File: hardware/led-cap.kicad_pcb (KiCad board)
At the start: 2 copper layers, 76.2 x 17.8 mm, 12 parts, among them IC1 ATTINY20-X, K1 CONN_3, P1 battery, P2 pgrm, Q1 IRLML2402PbF, U1 MMA7660

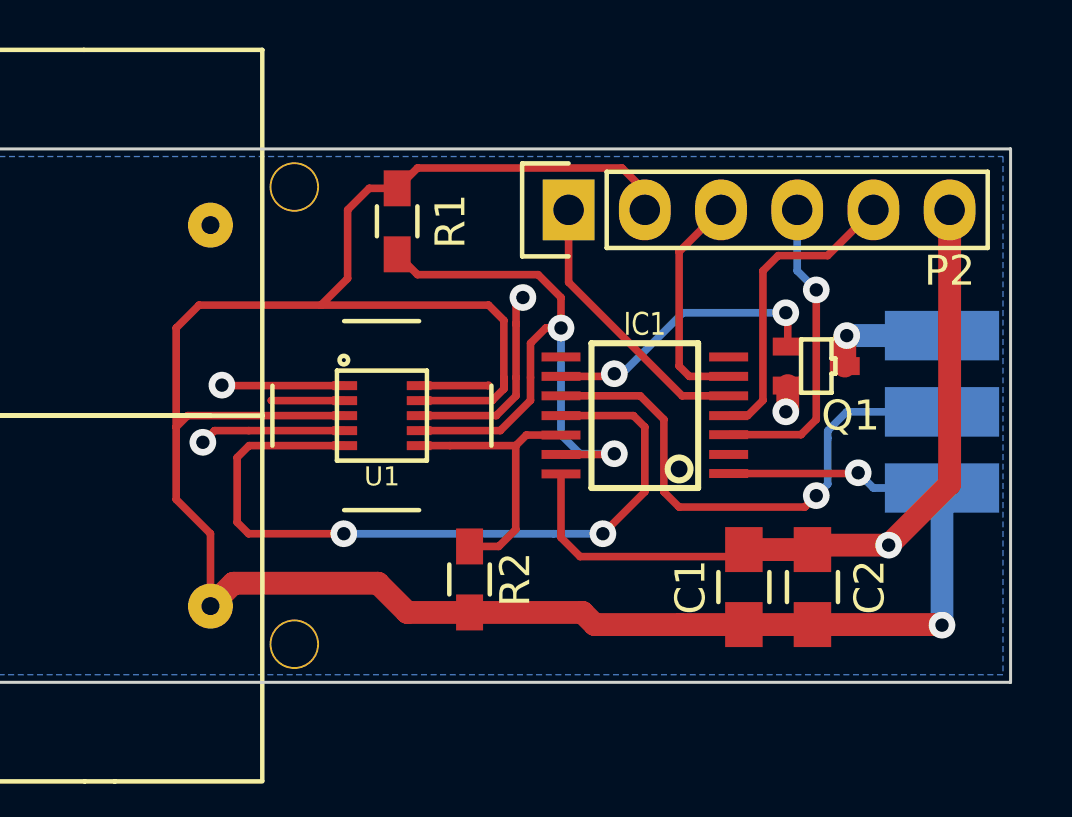
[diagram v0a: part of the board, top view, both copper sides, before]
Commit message: Fixing the mosfet
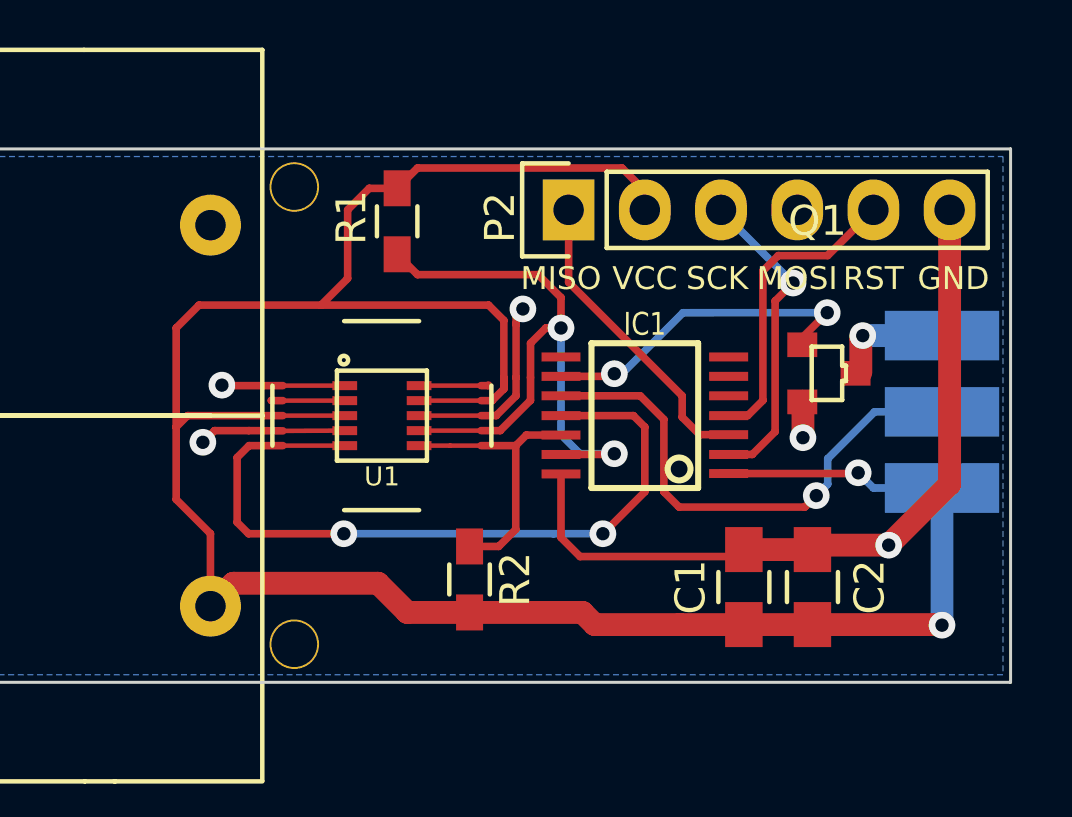
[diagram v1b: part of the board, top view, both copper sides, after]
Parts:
- P2: value pgrm -> TPI pgrm
- Q1: footprint SMD_Packages:SOT-323 -> mods.pretty:SOT-323-b
- moved Q1 1.33 mm to (187.9, 76.1), turned to 270 degrees
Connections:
- IC1 pad 2: Net-(IC1-Pad2) -> /CLOCK
- IC1 pad 3: /MOSI -> /DATA
- IC1 pad 5: /MISO -> Net-(IC1-Pad5)
- IC1 pad 6: /SCLK -> Net-(IC1-Pad6)
- P2 pad 1: /MISO -> /DATA
- P2 pad 3: /SCLK -> /CLOCK
- P2 pad 4: /MOSI -> Net-(P2-Pad4)
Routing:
- net /CLOCK: track 0.00 -> 10.5 mm, vias 0 -> 1
- net /MOSI: track 10.4 -> 0.00 mm, vias 1 -> 0
- net /DATA: track 0.00 -> 10.3 mm
- net /MISO: track 9.31 -> 0.00 mm
- net /SCLK: track 7.32 -> 0.00 mm
- net /LED_CTRL: track 9.65 -> 11.4 mm
- net /LED_DATA: track 20.5 -> 20.0 mm
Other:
- board text added: "GND"
- board text added: "MISO"
- board text added: "MOSI"
- board text added: "RST"
- board text added: "SCK"
- board text added: "VCC"

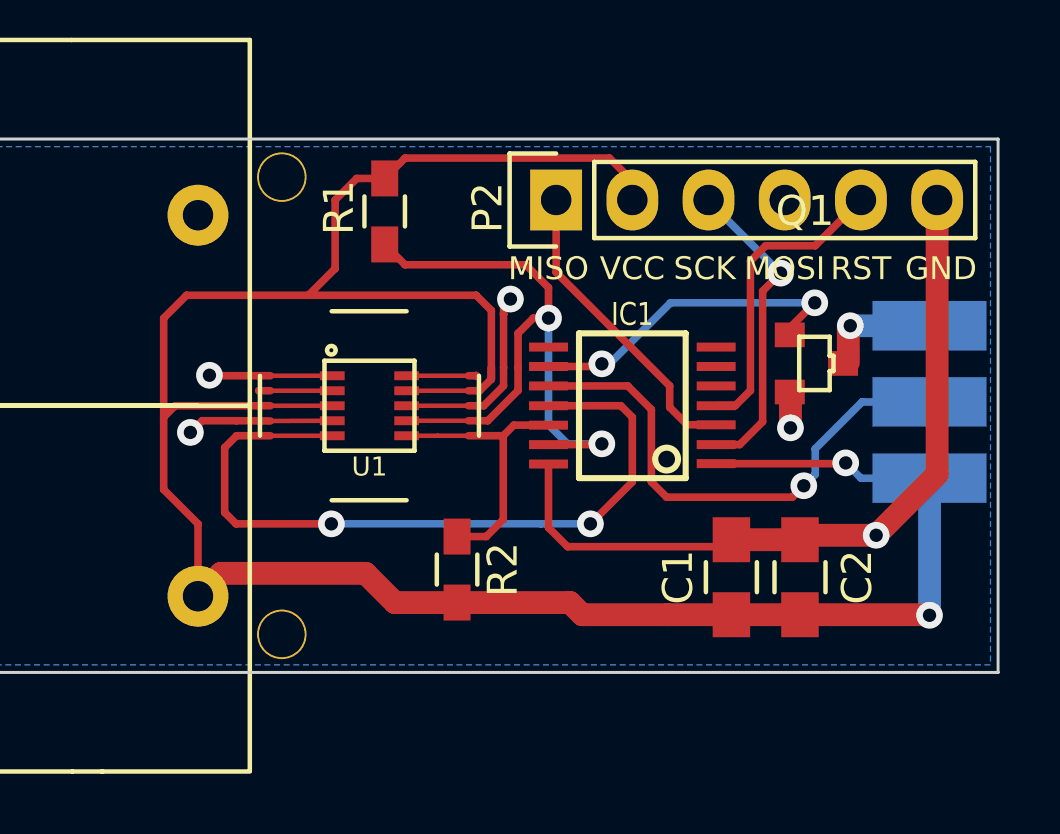
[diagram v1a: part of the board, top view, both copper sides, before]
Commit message: Fixed pcb and schematic for TPI and new LED strips
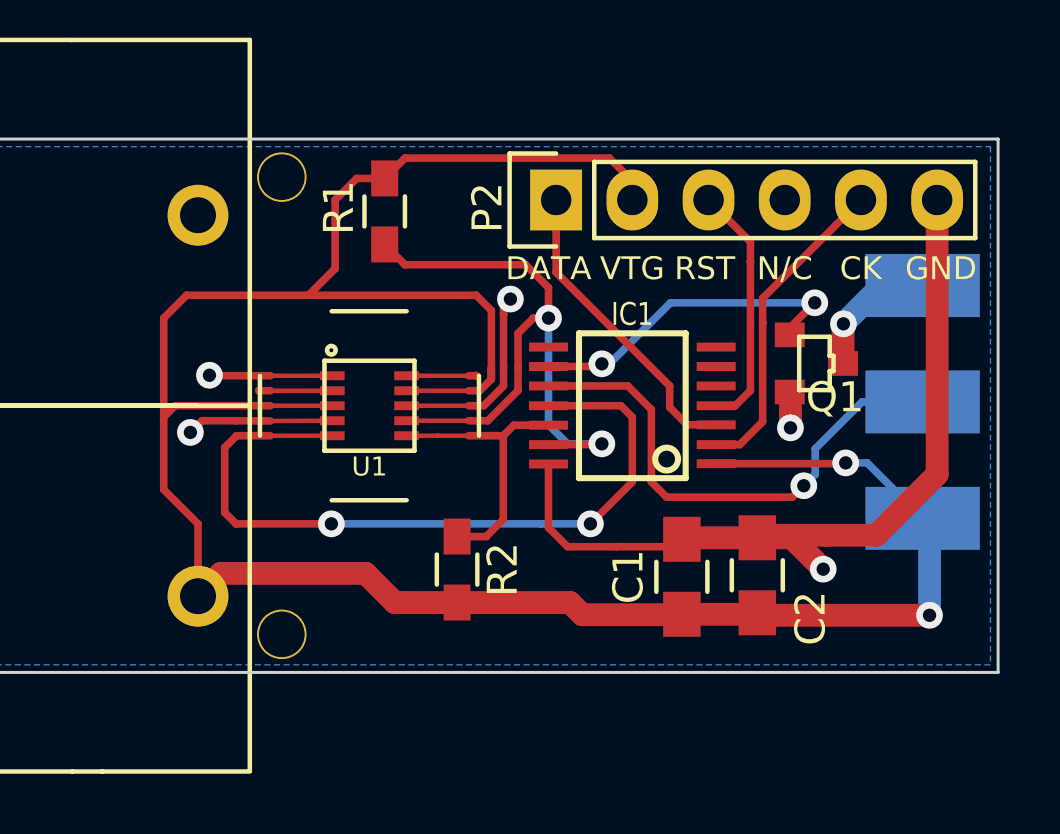
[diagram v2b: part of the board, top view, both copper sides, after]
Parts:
- K1: footprint mods.pretty:GS3 -> mods.pretty:LEDS
- moved C1 1.65 mm to (182.5, 83.2)
- moved C2 1.42 mm to (185.0, 83.1)
- moved K1 0.23 mm to (190.5, 77.3)
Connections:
- IC1 pad 2: /CLOCK -> /CLK
- P2 pad 3: /CLOCK -> /RST
- P2 pad 5: /RST -> /CLK
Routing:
- net /CLK: track 0.00 -> 10.7 mm
- net /CLOCK: track 10.5 -> 0.00 mm, vias 1 -> 0
- net GND: track 42.3 -> 44.9 mm
- net /RST: track 10.2 -> 8.35 mm
- net VCC: track 85.1 -> 84.3 mm
- net /LED_GND: track 3.90 -> 4.50 mm
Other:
- board text added: "CK"
- board text added: "DAT"
- board text added: "DATA"
- board text added: "N/C"
- board text added: "Spring 2015 Butler Fund"
- board text added: "UMAINE ECE 498"
- board text added: "VTG"
- board text removed: "MISO"
- board text removed: "MOSI"
- board text removed: "SCK"
- board text removed: "UMAINE ECE 498 Spring 2015 Butler Fund"

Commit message: Contains files as submitted to PCBCart
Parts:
- added 1pin: VAL**, mods.pretty:1pin, F.Cu at (191.8, 85.1)
- added 1pin: VAL**, mods.pretty:1pin, F.Cu at (118.7, 84.7)
- added 1pin: VAL**, mods.pretty:1pin, F.Cu at (118.8, 70.3)
- added 1pin: VAL**, mods.pretty:1pin, F.Cu at (142.5, 77.5)
- moved Q1 0.27 mm to (188.1, 76.0)
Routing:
- net VCC: track 84.3 -> 83.0 mm
- net /LED_CTRL: track 11.4 -> 10.4 mm
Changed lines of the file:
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@@
     (links 28)
     (no_connects 0)
-    (area 116.789999 68.529999 193.090001 86.410001)
+    (area 116.45569 65.050599 197.579962 89.889401)
     (thickness 1.6)
     (drawings 15)
     (tracks 177)
     (zones 0)
-    (modules 12)
+    (modules 16)
     (nets 19)
   )
@@
     (pcbplotparams
       (layerselection 0x010f0_80000001)
-      (usegerberextensions false)
+      (usegerberextensions true)
       (excludeedgelayer true)
       (linewidth 0.100000)
@@
     )
   )
-  (module mods.pretty:SOT-323-b placed (layer F.Cu)
-    (at 187.8711 76.0603 270)
-    (tags "SMD SOT")
-    (attr smd)
-    (fp_text reference Q1 (at 1.1303 0.2667 360) (layer F.SilkS)
-      (effects (font (size 1 1) (thickness 0.15)))
-    )
-    (fp_text value IRLML2402PbF (at 0 -3.81 270) (layer F.SilkS) hide
-      (effects (font (size 1 1) (thickness 0.15)))
-    )
-    (fp_line (start 0.254 0.4445) (end 0.889 0.4445) (layer F.SilkS) (width 0.15))
-    (fp_line (start 0.889 0.4445) (end 0.889 1.4605) (layer F.SilkS) (width 0.15))
-    (fp_line (start -0.889 1.4605) (end -0.889 0.4445) (layer F.SilkS) (width 0.15))
-    (fp_line (start -0.889 0.4445) (end -0.254 0.4445) (layer F.SilkS) (width 0.15))
-    (fp_line (start 0.254 0.3175) (end 0.254 0.4445) (layer F.SilkS) (width 0.15))
-    (fp_line (start -0.254 0.4445) (end -0.254 0.3175) (layer F.SilkS) (width 0.15))
-    (fp_line (start 0.889 1.4605) (end -0.889 1.4605) (layer F.SilkS) (width 0.15))
-    (fp_line (start -0.254 0.3175) (end 0.254 0.3175) (layer F.SilkS) (width 0.15))
-    (pad 2 smd rect (at 0.9525 1.77546 270) (size 0.82296 1.00076) (layers F.Cu F.Paste F.Mask)
-      (net 2 GND))
-    (pad 1 smd rect (at -0.9525 1.77546 270) (size 0.82296 1.00076) (layers F.Cu F.Paste F.Mask)
-      (net 6 /LED_CTRL))
-    (pad 3 smd rect (at 0 0 270) (size 0.82296 1.00076) (layers F.Cu F.Paste F.Mask)
-      (net 11 /LED_GND))
-    (model SMD_Packages/SOT-323.wrl
-      (at (xyz 0 0 0.001))
-      (scale (xyz 0.3937 0.3937 0.3937))
-      (rotate (xyz 0 0 0))
-    )
-  )
   (module mods.pretty:LEDS placed (layer B.Cu)
     (at 190.5254 77.343)
@@
     (pad 3 smd rect (at 0 -3.88) (size 3.81 2.1) (layers B.Cu B.Paste B.Mask)
       (net 11 /LED_GND))
+  )
+  (module mods.pretty:1pin (layer F.Cu)
+    (at 191.7827 85.09)
+    (descr "module 1 pin (ou trou mecanique de percage)")
+    (tags DEV)
+    (fp_text reference 1pin (at 0 -3.048) (layer F.SilkS) hide
+      (effects (font (size 1 1) (thickness 0.15)))
+    )
+    (fp_text value VAL** (at 0 2.794) (layer F.SilkS) hide
+      (effects (font (size 1 1) (thickness 0.15)))
+    )
+    (pad "" thru_hole circle (at 0 0) (size 1.651 1.651) (drill 1.524) (layers *.Cu *.Mask F.SilkS))
+  )
+  (module mods.pretty:1pin (layer F.Cu)
+    (at 118.7069 84.7344)
+    (descr "module 1 pin (ou trou mecanique de percage)")
+    (tags DEV)
+    (fp_text reference 1pin (at 0 -3.048) (layer F.SilkS) hide
+      (effects (font (size 1 1) (thickness 0.15)))
+    )
+    (fp_text value VAL** (at 0 2.794) (layer F.SilkS) hide
+      (effects (font (size 1 1) (thickness 0.15)))
+    )
+    (pad "" thru_hole circle (at 0 0) (size 1.651 1.651) (drill 1.524) (layers *.Cu *.Mask F.SilkS))
+  )
+  (module mods.pretty:1pin (layer F.Cu)
+    (at 118.7704 70.2691)
+    (descr "module 1 pin (ou trou mecanique de percage)")
+    (tags DEV)
+    (fp_text reference 1pin (at 0 -3.048) (layer F.SilkS) hide
+      (effects (font (size 1 1) (thickness 0.15)))
+    )
+    (fp_text value VAL** (at 0 2.794) (layer F.SilkS) hide
+      (effects (font (size 1 1) (thickness 0.15)))
+    )
+    (pad "" thru_hole circle (at 0 0) (size 1.651 1.651) (drill 1.524) (layers *.Cu *.Mask F.SilkS))
+  )
+  (module mods.pretty:1pin (layer F.Cu)
+    (at 142.494 77.5081)
+    (descr "module 1 pin (ou trou mecanique de percage)")
+    (tags DEV)
+    (fp_text reference 1pin (at 0 -3.048) (layer F.SilkS) hide
+      (effects (font (size 1 1) (thickness 0.15)))
+    )
+    (fp_text value VAL** (at 0 2.794) (layer F.SilkS) hide
+      (effects (font (size 1 1) (thickness 0.15)))
+    )
+    (pad "" thru_hole circle (at 0 0) (size 1.651 1.651) (drill 1.524) (layers *.Cu *.Mask F.SilkS))
+  )
+  (module mods.pretty:SOT-323-b placed (layer F.Cu)
+    (at 188.1378 76.0476 270)
+    (tags "SMD SOT")
+    (attr smd)
+    (fp_text reference Q1 (at -0.5842 -1.4732 360) (layer F.SilkS)
+      (effects (font (size 1 1) (thickness 0.15)))
+    )
+    (fp_text value IRLML2402PbF (at 0 -3.81 270) (layer F.SilkS) hide
+      (effects (font (size 1 1) (thickness 0.15)))
+    )
+    (fp_line (start 0.254 0.4445) (end 0.889 0.4445) (layer F.SilkS) (width 0.15))
+    (fp_line (start 0.889 0.4445) (end 0.889 1.4605) (layer F.SilkS) (width 0.15))
+    (fp_line (start -0.889 1.4605) (end -0.889 0.4445) (layer F.SilkS) (width 0.15))
+    (fp_line (start -0.889 0.4445) (end -0.254 0.4445) (layer F.SilkS) (width 0.15))
+    (fp_line (start 0.254 0.3175) (end 0.254 0.4445) (layer F.SilkS) (width 0.15))
+    (fp_line (start -0.254 0.4445) (end -0.254 0.3175) (layer F.SilkS) (width 0.15))
+    (fp_line (start 0.889 1.4605) (end -0.889 1.4605) (layer F.SilkS) (width 0.15))
+    (fp_line (start -0.254 0.3175) (end 0.254 0.3175) (layer F.SilkS) (width 0.15))
+    (pad 2 smd rect (at 0.9525 1.77546 270) (size 0.82296 1.50076) (layers F.Cu F.Paste F.Mask)
+      (net 2 GND))
+    (pad 1 smd rect (at -0.9525 1.77546 270) (size 0.82296 1.50076) (layers F.Cu F.Paste F.Mask)
+      (net 6 /LED_CTRL))
+    (pad 3 smd rect (at 0 0 270) (size 0.82296 1.50076) (layers F.Cu F.Paste F.Mask)
+      (net 11 /LED_GND))
+    (model SMD_Packages/SOT-323.wrl
+      (at (xyz 0 0 0.001))
+      (scale (xyz 0.3937 0.3937 0.3937))
+      (rotate (xyz 0 0 0))
+    )
   )
   (gr_text VCC (at 187.1472 81.4324) (layer B.SilkS)
@@
   (segment (start 187.9346 79.4004) (end 187.96 79.375) (width 0.254) (layer F.Cu) (net 1))
   (segment (start 187.96 79.375) (end 188.6774 79.375) (width 0.254) (layer B.Cu) (net 1))
-  (via (at 190.754 84.455) (size 0.889) (layers F.Cu B.Cu) (net 1))
-  (segment (start 190.754 84.455) (end 190.734 84.435) (width 0.762) (layer F.Cu) (net 1))
-  (segment (start 190.754 81.4516) (end 190.754 84.455) (width 0.762) (layer B.Cu) (net 1))
+  (via (at 189.0268 84.455) (size 0.889) (layers F.Cu B.Cu) (net 1))
+  (segment (start 189.0268 84.455) (end 189.0068 84.435) (width 0.762) (layer F.Cu) (net 1))
+  (segment (start 190.754 81.4516) (end 189.0268 84.455) (width 0.762) (layer B.Cu) (net 1))
   (segment (start 185.0971 84.455) (end 185.0136 84.3715) (width 0.762) (layer F.Cu) (net 1))
-  (segment (start 190.754 84.455) (end 185.0971 84.455) (width 0.762) (layer F.Cu) (net 1))
+  (segment (start 189.0268 84.455) (end 185.0971 84.455) (width 0.762) (layer F.Cu) (net 1))
   (segment (start 182.5498 84.3715) (end 182.499 84.4223) (width 0.762) (layer F.Cu) (net 1))
   (segment (start 182.4863 84.435) (end 182.499 84.4223) (width 0.762) (layer F.Cu) (net 1))
@@
   (segment (start 184.9628 84.4223) (end 185.0136 84.3715) (width 0.762) (layer F.Cu) (net 1))
   (segment (start 182.499 84.4223) (end 184.9628 84.4223) (width 0.762) (layer F.Cu) (net 1))
+  (segment (start 186.09564 78.64094) (end 186.1058 78.6511) (width 0.254) (layer F.Cu) (net 2))
+  (via (at 186.1058 78.6511) (size 0.889) (layers F.Cu B.Cu) (net 2))
+  (segment (start 186.1058 78.6511) (end 186.1058 78.6765) (width 0.254) (layer B.Cu) (net 2))
+  (segment (start 186.1185 77.0001) (end 186.10834 76.98994) (width 0.762) (layer F.Cu) (net 2))
+  (segment (start 186.1058 78.6511) (end 186.1185 77.0001) (width 0.762) (layer F.Cu) (net 2))
   (segment (start 166.767 76.47) (end 166.751 76.454) (width 0.254) (layer F.Cu) (net 2))
   (via (at 166.751 76.454) (size 0.889) (layers F.Cu B.Cu) (net 2))
@@
   (via (at 176.784 73.914) (size 0.889) (layers F.Cu B.Cu) (net 2))
   (segment (start 176.555402 74.422) (end 176.555402 74.142598) (width 0.254) (layer F.Cu) (net 2))
-  (segment (start 186.10834 78.19644) (end 186.1185 78.2066) (width 0.254) (layer F.Cu) (net 2))
-  (via (at 186.1185 78.2066) (size 0.889) (layers F.Cu B.Cu) (net 2))
-  (segment (start 186.1185 78.2066) (end 186.1185 78.232) (width 0.254) (layer B.Cu) (net 2))
-  (segment (start 186.1185 77.0001) (end 186.10834 76.98994) (width 0.762) (layer F.Cu) (net 2))
-  (segment (start 186.1185 78.2066) (end 186.1185 77.0001) (width 0.762) (layer F.Cu) (net 2))
   (segment (start 185.0971 81.788) (end 185.0136 81.8715) (width 0.762) (layer F.Cu) (net 2))
   (segment (start 191.008 79.756) (end 188.976 81.788) (width 0.762) (layer F.Cu) (net 2))
@@
   (via (at 179.832 76.073) (size 0.889) (layers F.Cu B.Cu) (net 6))
   (segment (start 180.086 76.073) (end 182.118 74.041) (width 0.254) (layer B.Cu) (net 6))
-  (segment (start 186.92876 74.03846) (end 182.118 74.041) (width 0.254) (layer B.Cu) (net 6))
-  (via (at 186.92876 74.03846) (size 0.889) (layers F.Cu B.Cu) (net 6))
-  (segment (start 186.9948 74.1045) (end 186.92876 74.03846) (width 0.254) (layer F.Cu) (net 6))
+  (segment (start 186.2963 74.041) (end 182.118 74.041) (width 0.254) (layer B.Cu) (net 6))
+  (via (at 186.2963 74.041) (size 0.889) (layers F.Cu B.Cu) (net 6))
+  (segment (start 186.36234 74.10704) (end 186.2963 74.041) (width 0.254) (layer F.Cu) (net 6))
   (segment (start 179.832 76.073) (end 180.086 76.073) (width 0.254) (layer B.Cu) (net 6))
-  (segment (start 186.09564 74.87158) (end 186.92876 74.03846) (width 0.254) (layer F.Cu) (net 6))
+  (segment (start 186.09564 74.87158) (end 186.2963 74.041) (width 0.254) (layer F.Cu) (net 6))
   (segment (start 186.09564 75.1078) (end 186.09564 74.87158) (width 0.254) (layer F.Cu) (net 6))
   (segment (start 190.754 77.343) (end 189.611 77.343) (width 0.254) (layer B.Cu) (net 7))
